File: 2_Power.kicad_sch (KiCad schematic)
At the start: 0 parts

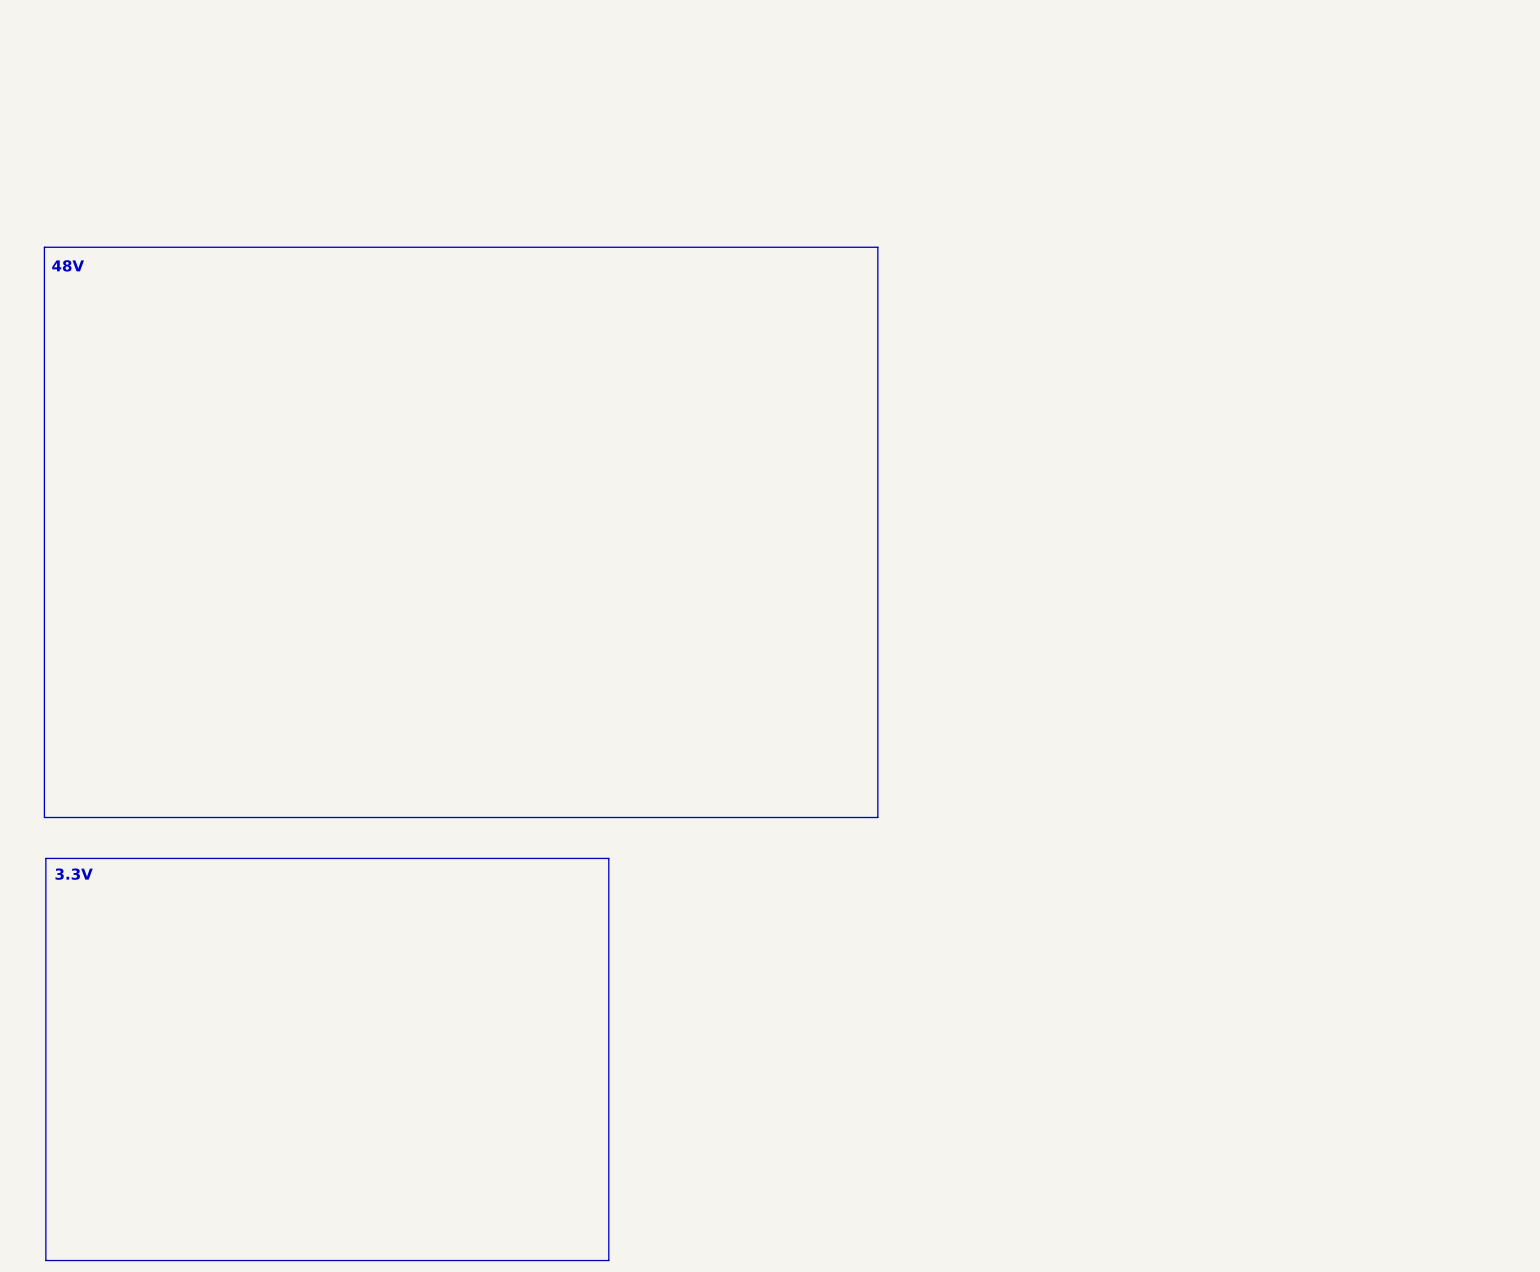
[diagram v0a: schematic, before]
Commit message: Add boost converter
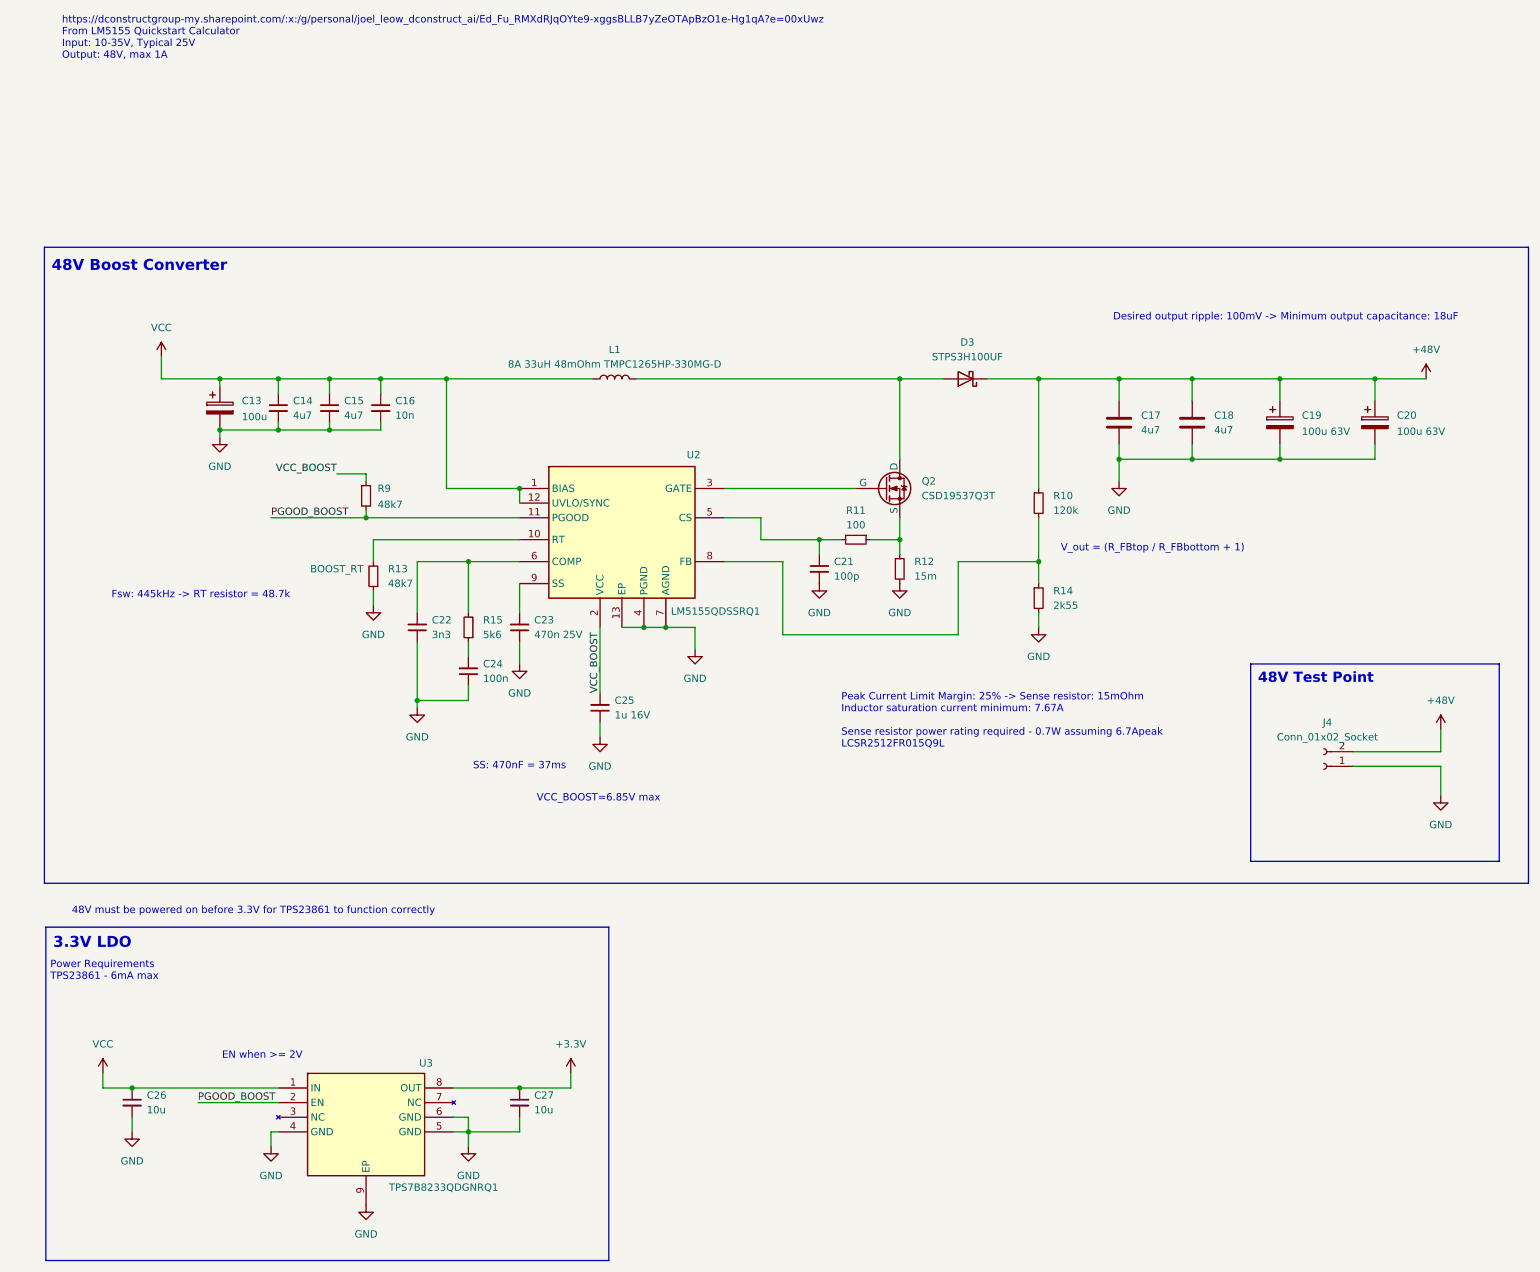
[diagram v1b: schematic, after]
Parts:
- added C13: 100u, Capacitor_SMD:C_Elec_10x10.2, symbol Device:C_Polarized
- added C14, C15: 4u7, symbol Device:C_Small
- added C16: 10n, symbol Device:C_Small
- added C17, C18: 4u7, symbol Device:C
- added C19, C20: 100u 63V, Capacitor_SMD:C_Elec_10x10.2, symbol Device:C_Polarized
- added C21: 100p, symbol Device:C_Small
- added C22: 3n3, Resistor_SMD:R_0402_1005Metric, symbol Device:C_Small
- added C23: 470n 25V, symbol Device:C_Small
- added C24: 100n, symbol Device:C_Small
- added C25: 1u 16V, symbol Device:C_Small
- added C26, C27: 10u, symbol Device:C_Small
- added D3: STPS3H100UF, symbol Device:D_Schottky
- added J4: Conn_01x02_Socket, symbol Connector:Conn_01x02_Socket
- added L1: 8A 33uH 48mOhm TMPC1265HP-330MG-D, symbol Device:L
- added Q2: CSD19537Q3T, symbol Simulation_SPICE:NMOS
- added R10: 120k, Resistor_SMD:R_0603_1608Metric, symbol Device:R_Small
- added R11: 100, Resistor_SMD:R_0603_1608Metric, symbol Device:R_Small
- added R12: 15m, Resistor_SMD:R_2512_6332Metric, symbol Device:R_Small
- added R13, R9: 48k7, Resistor_SMD:R_0402_1005Metric, symbol Device:R_Small
- added R14: 2k55, Resistor_SMD:R_0603_1608Metric, symbol Device:R_Small
- added R15: 5k6, Resistor_SMD:R_0402_1005Metric, symbol Device:R_Small
- added U2: LM5155QDSSRQ1, SON50P200X300X80-13N, symbol CakeKiCadLib:LM5155QDSSRQ1
- added U3: TPS7B8233QDGNRQ1, CakeKiCadLib:TPS7B8233QDGNRQ1, symbol CakeKiCadLib:TPS7B8233QDGNRQ1
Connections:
- new net: D3.2 (A), L1.2, Q2.1 (D)
- new net: Q2.2 (G), U2.3 (GATE)
- new net: Q2.3 (S), R11.1, R12.1
- new net: R10.2, R14.1, U2.8 (FB)
- new net: C21.1, R11.2, U2.5 (CS)
- new net: C23.2, U2.9 (SS)
- new net: C24.2, R15.1
- new net: C22.2, R15.2, U2.6 (COMP)
- new net: R13.2, U2.10 (RT)
- new net +3.3V: C27.1, U3.8 (OUT)
- new net +48V: C17.1, C18.1, C19.1, C20.1, D3.1 (K), J4.2 (Pin_2), R10.1
- new net GND: C13.2, C14.2, C15.2, C16.2, C17.2, C18.2, C19.2, C20.2, C21.2, C22.1, C23.1, C24.1, C25.1, C26.2, C27.2, J4.1 (Pin_1), R12.2, R13.1, R14.2, U2.13 (EP), U2.4 (PGND), U2.7 (AGND), U3.4 (GND), U3.5 (GND), U3.6 (GND), U3.9 (EP)
- new net PGOOD_BOOST: R9.2, U2.11 (PGOOD), U3.2 (EN)
- new net VCC: C13.1, C14.1, C15.1, C16.1, C26.1, L1.1, U2.1 (BIAS), U2.12 (UVLO/SYNC), U3.1 (IN)
- new net VCC_BOOST: C25.2, R9.1, U2.2 (VCC)
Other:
- note added: "3.3V LDO"
- note added: "48V Boost Converter"
- note added: "48V Test Point"
- note added: "48V must be powered on before 3.3V for TPS23861 to function correctly"
- note added: "Desired output ripple: 100mV -> Minimum output capacitance: 18uF"
- note added: "EN when >= 2V"
- note added: "Fsw: 445kHz -> RT resistor = 48.7k"
- note added: "Peak Current Limit Margin: 25% -> Sense resistor: 15mOhm Inductor saturation current minimum: 7.67A Sense resistor power rating required - 0.7W assuming 6.7Apeak LCSR2512FR015Q9L"
- note added: "Power Requirements TPS23861 - 6mA max"
- note added: "SS: 470nF = 37ms"
- note added: "VCC_BOOST=6.85V max"
- note added: "V_out = (R_FBtop / R_FBbottom + 1)"
- note added: "https://dconstructgroup-my.sharepoint.com/:x:/g/personal/joel_leow_dconstruct_ai/Ed_Fu_RMXdRJqOYte9-xggsBLLB7yZeOTApBzO1e-Hg1qA?e=00xUwz From LM5155 Quickstart Calculator Input: 10-35V, Typical 25V Output: 48V, max 1A"
- note removed: "3.3V"
- note removed: "48V"

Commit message: finish layout
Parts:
- removed C13: 100u, Capacitor_SMD:C_Elec_10x10.2, symbol Device:C_Polarized
- removed C15: 4u7, symbol Device:C_Small
- removed C18: 4u7, symbol Device:C
- removed C20: 100u 63V, Capacitor_SMD:C_Elec_10x10.2, symbol Device:C_Polarized
- removed C27: 10u, symbol Device:C_Small
- added C14: 68u, CakeKiCadLib:CP_Elec_12.5x13.5, symbol Device:C_Polarized
- added C16: 4u7, Capacitor_SMD:C_1206_3216Metric, symbol Device:C_Small
- added C19: 4u7 100V, Capacitor_SMD:C_1210_3225Metric, symbol Device:C
- added C21: 68u 100V, CakeKiCadLib:CP_Elec_12.5x13.5, symbol Device:C_Polarized
- added C28: 10u, Capacitor_SMD:C_0805_2012Metric, symbol Device:C_Small
- added C29: 1u, Capacitor_SMD:C_0805_2012Metric, symbol Device:C_Small
- added D4: LED, LED_SMD:LED_0603_1608Metric, symbol Device:LED
- added R20: 2k26, Resistor_SMD:R_0603_1608Metric, symbol Device:R_Small
- added R21: 48k7, Resistor_SMD:R_0402_1005Metric, symbol Device:R_Small
- C15: renamed from C14; footprint (none) -> Capacitor_SMD:C_1206_3216Metric; LCSC (none) -> C29823
- C17: renamed from C16; footprint (none) -> Capacitor_SMD:C_0603_1608Metric; LCSC (none) -> C57112
- C18: renamed from C17; value 4u7 -> 4u7 100V; footprint (none) -> Capacitor_SMD:C_1210_3225Metric; LCSC (none) -> C381466
- C20: renamed from C19; value 100u 63V -> 68u 100V; footprint Capacitor_SMD:C_Elec_10x10.2 -> CakeKiCadLib:CP_Elec_12.5x13.5; LCSC C128460 -> C278544
- C22: renamed from C21; footprint (none) -> Capacitor_SMD:C_0402_1005Metric
- C23: renamed from C22; value 3n3 -> 1n5; footprint Resistor_SMD:R_0402_1005Metric -> Resistor_SMD:R_0603_1608Metric; LCSC C107028 -> C1595
- C24: renamed from C23; footprint (none) -> Capacitor_SMD:C_0603_1608Metric
- C25: renamed from C24; footprint (none) -> Resistor_SMD:R_0603_1608Metric; LCSC (none) -> C14663
- C26: renamed from C25; value 1u 16V -> 1u; footprint (none) -> Capacitor_SMD:C_0805_2012Metric; LCSC C29266 -> C28323
- C27: renamed from C26; footprint (none) -> Capacitor_SMD:C_0805_2012Metric; LCSC (none) -> C440198
- D3: footprint (none) -> CakeKiCadLib:D_SMBflat
- J4: value Conn_01x02_Socket -> 54V Test Points; footprint (none) -> Connector_Wire:SolderWire-2.5sqmm_1x02_P8.8mm_D2.4mm_OD4.4mm
- L1: value 8A 33uH 48mOhm TMPC1265HP-330MG-D -> 9A 22uH 37mOhm TMPC1265HP-220MG-D; footprint (none) -> Inductor_SMD:L_TaiTech_TMPC1265_13.5x12.5mm; LCSC C2880059 -> C305224
- Q2: footprint (none) -> CakeKiCadLib:CSD19537Q3T
- R18: renamed from R14; value 2k55 -> 2k26; LCSC C25965 -> C22904
- R19: renamed from R15; value 5k6 -> 5k76; footprint Resistor_SMD:R_0402_1005Metric -> Resistor_SMD:R_0603_1608Metric; LCSC C156115 -> C23070
- U2: footprint SON50P200X300X80-13N -> CakeKiCadLib:LM5155QDSSRQ1
- renumbered R9 to R13, R10 to R14, R11 to R15, R12 to R16, R13 to R17
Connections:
- net +3.3V: now also C28.1
- net GND: now also C14.2, C16.2, C19.2, C21.2, C28.2, C29.1, R20.2
- net PGOOD_BOOST: now also D4.2 (A), R21.1; no longer U3.2 (EN)
- net VCC: now also C14.1, C16.1
- net +48V renamed +54V
- net +54V: now also C19.1, C21.1
- new net: D4.1 (K), R20.1
- new net: C29.2, R21.2, U3.2 (EN)
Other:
- note added: "54V Boost Converter"
- note added: "54V Test Point"
- note added: "Add some RC delay to enable LDO"
- note added: "EN when >= 2V Simple delay circuit (RC = 49ms)"
- note added: "LED"
- note removed: "48V Boost Converter"
- note removed: "48V Test Point"
- note removed: "EN when >= 2V"
- moved on the sheet: C20, C27, J4, U3

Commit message: Some cleanups
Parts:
- removed Q2: CSD19537Q3T, CakeKiCadLib:CSD19537Q3T, symbol Simulation_SPICE:NMOS
- added Q2: CSD19537Q3T, CakeKiCadLib:CSD19537Q3T, symbol Device:Q_NMOS_SGD
- U2: footprint CakeKiCadLib:LM5155QDSSRQ1 -> CakeKiCadLib:DSS0012x
- U3: footprint CakeKiCadLib:TPS7B8233QDGNRQ1 -> CakeKiCadLib:DGN0008G
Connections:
- net at D3.2 (A), L1.2: now also Q2.3 (D)
- net at U2.3 (GATE): now also Q2.2 (G)
- net at R15.1, R16.1: now also Q2.1 (S)
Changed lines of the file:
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@@
 	)
 	(symbol
-		(lib_id "Simulation_SPICE:NMOS")
-		(at 163.83 58.42 0)
-		(unit 1)
-		(exclude_from_sim no)
-		(in_bom yes)
-		(on_board yes)
-		(dnp no)
-		(fields_autoplaced yes)
-		(property "Reference" "Q2"
-			(at 170.18 57.1499 0)
-			(effects
-				(font
-					(size 1.27 1.27)
-				)
-				(justify left)
-			)
-		)
-		(property "Value" "CSD19537Q3T"
-			(at 170.18 59.6899 0)
-			(effects
-				(font
-					(size 1.27 1.27)
-				)
-				(justify left)
-			)
-		)
-		(property "Footprint" "CakeKiCadLib:CSD19537Q3T"
-			(at 168.91 55.88 0)
-			(effects
-				(font
-					(size 1.27 1.27)
-				)
-				(hide yes)
-			)
-		)
-		(property "Datasheet" "https://ngspice.sourceforge.io/docs/ngspice-html-manual/manual.xhtml#cha_MOSFETs"
-			(at 163.83 71.12 0)
-			(effects
-				(font
-					(size 1.27 1.27)
-				)
-				(hide yes)
-			)
-		)
-		(property "Description" "N-MOSFET transistor, drain/source/gate"
-			(at 163.83 58.42 0)
-			(effects
-				(font
-					(size 1.27 1.27)
-				)
-				(hide yes)
-			)
-		)
-		(property "Sim.Device" "NMOS"
-			(at 163.83 75.565 0)
-			(effects
-				(font
-					(size 1.27 1.27)
-				)
-				(hide yes)
-			)
-		)
-		(property "Sim.Type" "VDMOS"
-			(at 163.83 77.47 0)
-			(effects
-				(font
-					(size 1.27 1.27)
-				)
-				(hide yes)
-			)
-		)
-		(property "Sim.Pins" "1=D 2=G 3=S"
-			(at 163.83 73.66 0)
-			(effects
-				(font
-					(size 1.27 1.27)
-				)
-				(hide yes)
-			)
-		)
-		(pin "3"
-		)
-		(pin "1"
-		)
-		(pin "2"
-		)
-		(instances
-			(project ""
-				(path "/9be6f327-e3ac-4f6a-b806-3c33632f054c/5a65d563-705d-4f9b-9056-b0661b705802"
-					(reference "Q2")
-					(unit 1)
-				)
-			)
-		)
-	)
-	(symbol
 		(lib_id "Device:R_Small")
 		(at 190.5 60.96 0)
@@
 			)
 		)
-		(property "Footprint" "CakeKiCadLib:TPS7B8233QDGNRQ1"
+		(property "Footprint" "CakeKiCadLib:DGN0008G"
 			(at 124.46 262.56 0)
 			(effects
@@
 	)
 	(symbol
+		(lib_id "Device:Q_NMOS_SGD")
+		(at 163.83 58.42 0)
+		(unit 1)
+		(exclude_from_sim no)
+		(in_bom yes)
+		(on_board yes)
+		(dnp no)
+		(fields_autoplaced yes)
+		(property "Reference" "Q2"
+			(at 170.18 57.1499 0)
+			(effects
+				(font
+					(size 1.27 1.27)
+				)
+				(justify left)
+			)
+		)
+		(property "Value" "CSD19537Q3T"
+			(at 170.18 59.6899 0)
+			(effects
+				(font
+					(size 1.27 1.27)
+				)
+				(justify left)
+			)
+		)
+		(property "Footprint" "CakeKiCadLib:CSD19537Q3T"
+			(at 168.91 55.88 0)
+			(effects
+				(font
+					(size 1.27 1.27)
+				)
+				(hide yes)
+			)
+		)
+		(property "Datasheet" "~"
+			(at 163.83 58.42 0)
+			(effects
+				(font
+					(size 1.27 1.27)
+				)
+				(hide yes)
+			)
+		)
+		(property "Description" "N-MOSFET transistor, source/gate/drain"
+			(at 163.83 58.42 0)
+			(effects
+				(font
+					(size 1.27 1.27)
+				)
+				(hide yes)
+			)
+		)
+		(pin "2"
+		)
+		(pin "1"
+		)
+		(pin "3"
+		)
+		(instances
+			(project ""
+				(path "/9be6f327-e3ac-4f6a-b806-3c33632f054c/5a65d563-705d-4f9b-9056-b0661b705802"
+					(reference "Q2")
+					(unit 1)
+				)
+			)
+		)
+	)
+	(symbol
 		(lib_id "Device:R_Small")
 		(at 62.23 165.1 90)
@@
 			)
 		)
-		(property "Footprint" "CakeKiCadLib:LM5155QDSSRQ1"
+		(property "Footprint" "CakeKiCadLib:DSS0012x"
 			(at 149.86 159.69 0)
 			(effects
